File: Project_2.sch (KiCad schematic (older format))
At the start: 0 parts

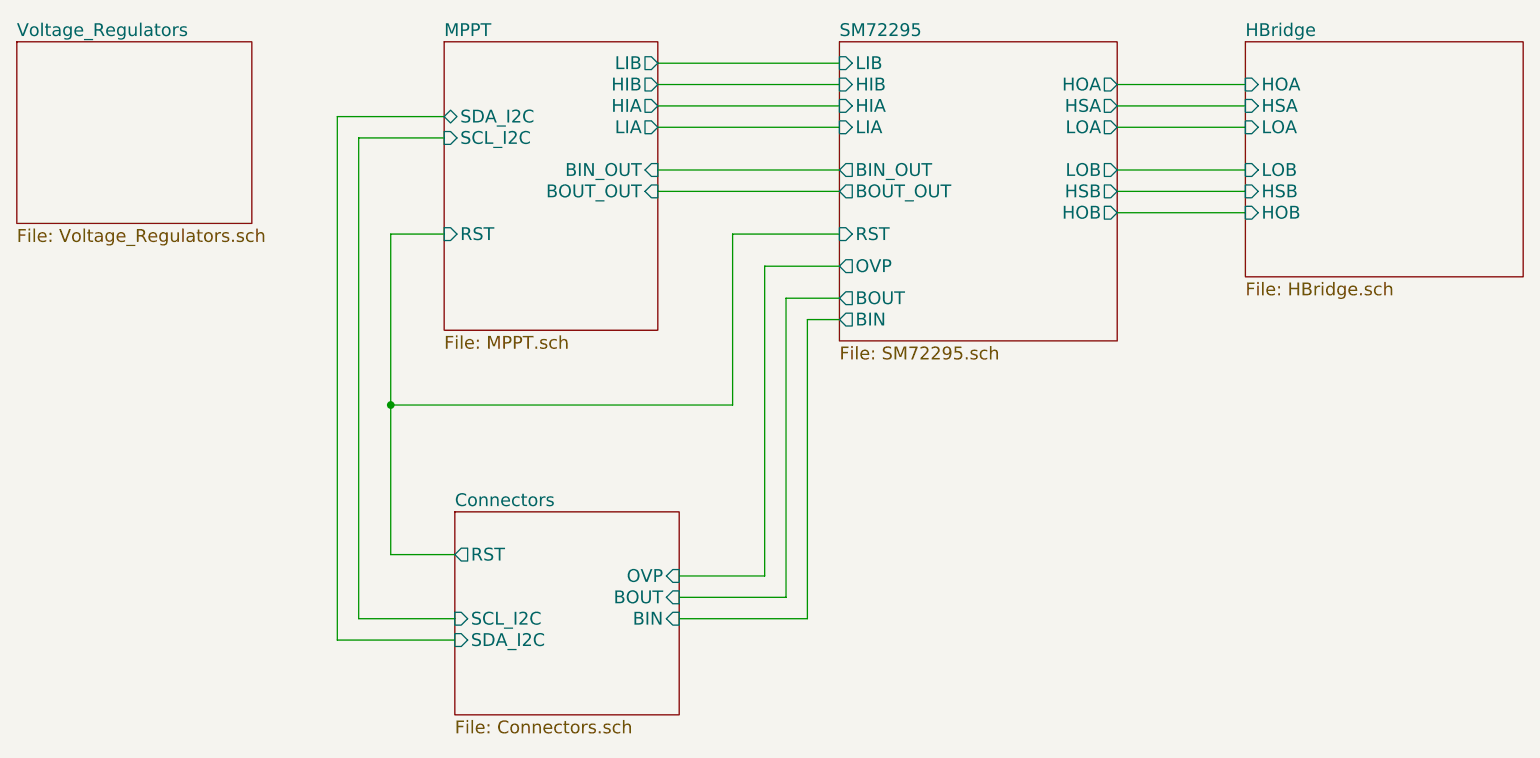
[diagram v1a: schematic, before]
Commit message: Routing done, prepping for DRC
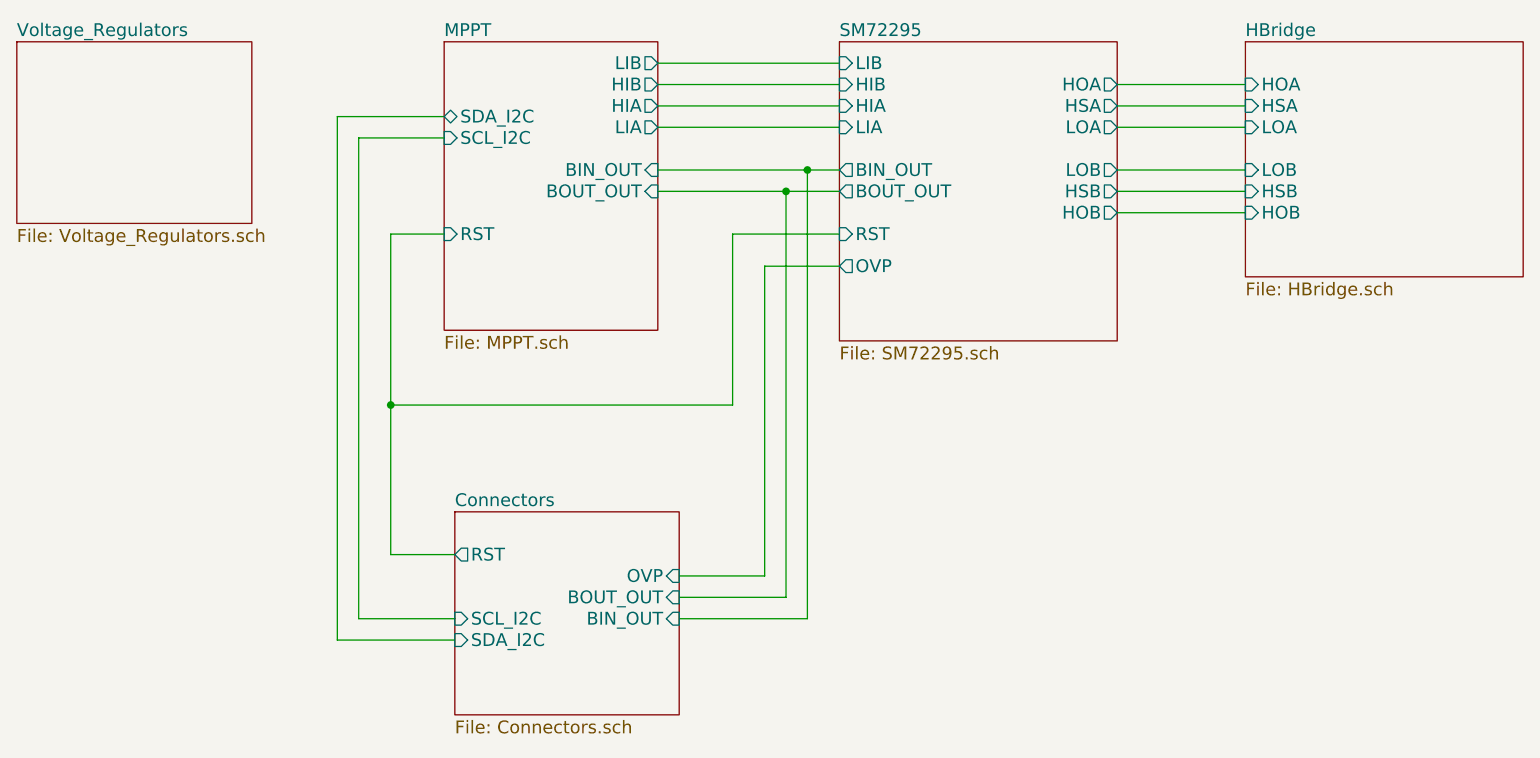
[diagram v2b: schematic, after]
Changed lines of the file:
@@
 F7 "BOUT_OUT" O L 5500 2200 60
 F8 "RST" I L 5500 2400 60
-F9 "BOUT" O L 5500 2700 60
-F10 "HOA" O R 6800 1700 60
-F11 "HSA" O R 6800 1800 60
-F12 "LOA" O R 6800 1900 60
-F13 "LOB" O R 6800 2100 60
-F14 "HSB" O R 6800 2200 60
-F15 "HOB" O R 6800 2300 60
-F16 "OVP" O L 5500 2550 60
-F17 "BIN" O L 5500 2800 60
+F9 "HOA" O R 6800 1700 60
+F10 "HSA" O R 6800 1800 60
+F11 "LOA" O R 6800 1900 60
+F12 "LOB" O R 6800 2100 60
+F13 "HSB" O R 6800 2200 60
+F14 "HOB" O R 6800 2300 60
+F15 "OVP" O L 5500 2550 60
 $EndSheet
 Wire Wire Line
@@
 Wire Wire Line
 	6800 2300 7400 2300
-$Sheet
-S 3700 3700 1050 950
-U 54F28AAE
-F0 "Connectors" 60
-F1 "Connectors.sch" 60
-F2 "RST" O L 3700 3900 60
-F3 "SDA_I2C" I L 3700 4300 60
-F4 "SCL_I2C" I L 3700 4200 60
-F5 "OVP" I R 4750 4000 60
-F6 "BIN" I R 4750 4200 60
-F7 "BOUT" I R 4750 4100 60
-$EndSheet
 Wire Wire Line
 	3400 3900 3700 3900
@@
 	5150 4000 4750 4000
 Wire Wire Line
-	5350 2800 5350 4200
-Wire Wire Line
-	5350 2800 5500 2800
+	5350 2100 5350 4200
 Wire Wire Line
 	5350 4200 4750 4200
 Wire Wire Line
-	4750 4100 5250 4100
+	5250 4100 4750 4100
 Wire Wire Line
-	5250 4100 5250 2700
-Wire Wire Line
-	5250 2700 5500 2700
+	5250 2200 5250 4100
+$Sheet
+S 3700 3700 1050 950
+U 54F28AAE
+F0 "Connectors" 60
+F1 "Connectors.sch" 60
+F2 "RST" O L 3700 3900 60
+F3 "SDA_I2C" I L 3700 4300 60
+F4 "SCL_I2C" I L 3700 4200 60
+F5 "OVP" I R 4750 4000 60
+F6 "BIN_OUT" I R 4750 4200 60
+F7 "BOUT_OUT" I R 4750 4100 60
+$EndSheet
+Connection ~ 5250 2200
+Connection ~ 5350 2100
 $EndSCHEMATC

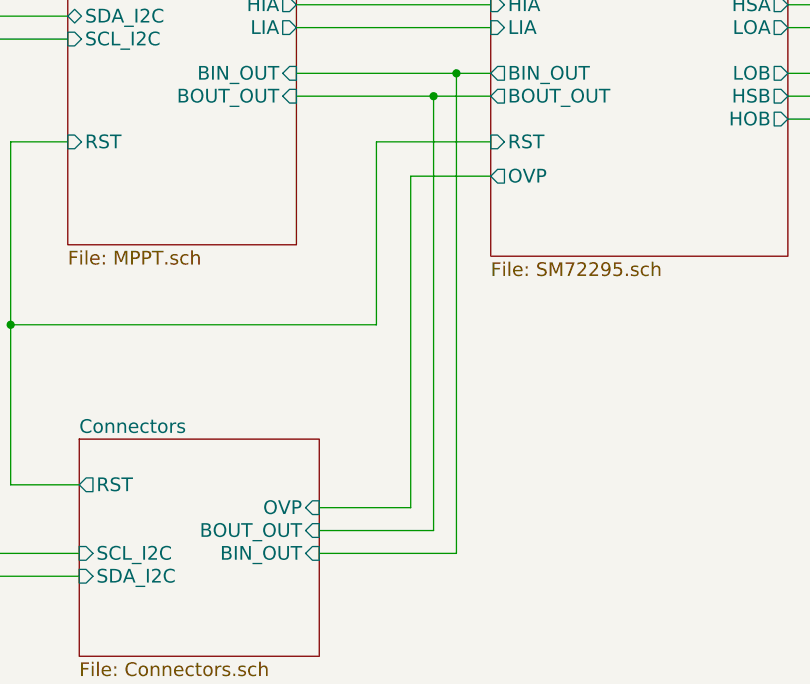
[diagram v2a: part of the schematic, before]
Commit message: Cleared all DRC errors.
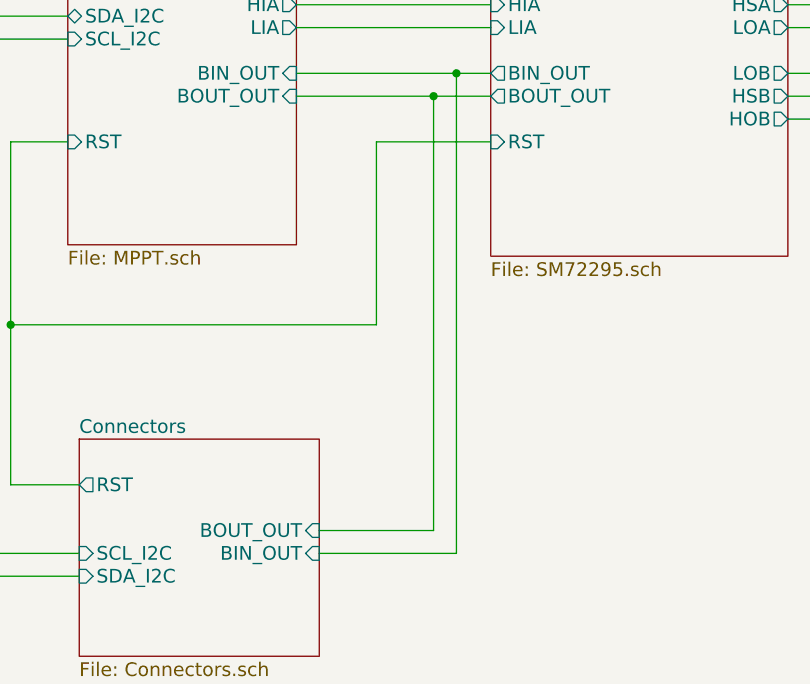
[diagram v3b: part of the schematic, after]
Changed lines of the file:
@@
 F13 "HSB" O R 6800 2200 60
 F14 "HOB" O R 6800 2300 60
-F15 "OVP" O L 5500 2550 60
 $EndSheet
 Wire Wire Line
@@
 	3150 1850 3650 1850
 Wire Wire Line
-	5150 4000 5150 2550
-Wire Wire Line
-	5150 2550 5500 2550
-Wire Wire Line
-	5150 4000 4750 4000
-Wire Wire Line
 	5350 2100 5350 4200
 Wire Wire Line
@@
 F3 "SDA_I2C" I L 3700 4300 60
 F4 "SCL_I2C" I L 3700 4200 60
-F5 "OVP" I R 4750 4000 60
-F6 "BIN_OUT" I R 4750 4200 60
-F7 "BOUT_OUT" I R 4750 4100 60
+F5 "BIN_OUT" I R 4750 4200 60
+F6 "BOUT_OUT" I R 4750 4100 60
 $EndSheet
 Connection ~ 5250 2200
